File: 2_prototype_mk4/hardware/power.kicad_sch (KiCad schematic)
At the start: 8 parts, among them J2 Conn_01x04_Pin, J6 171825-4

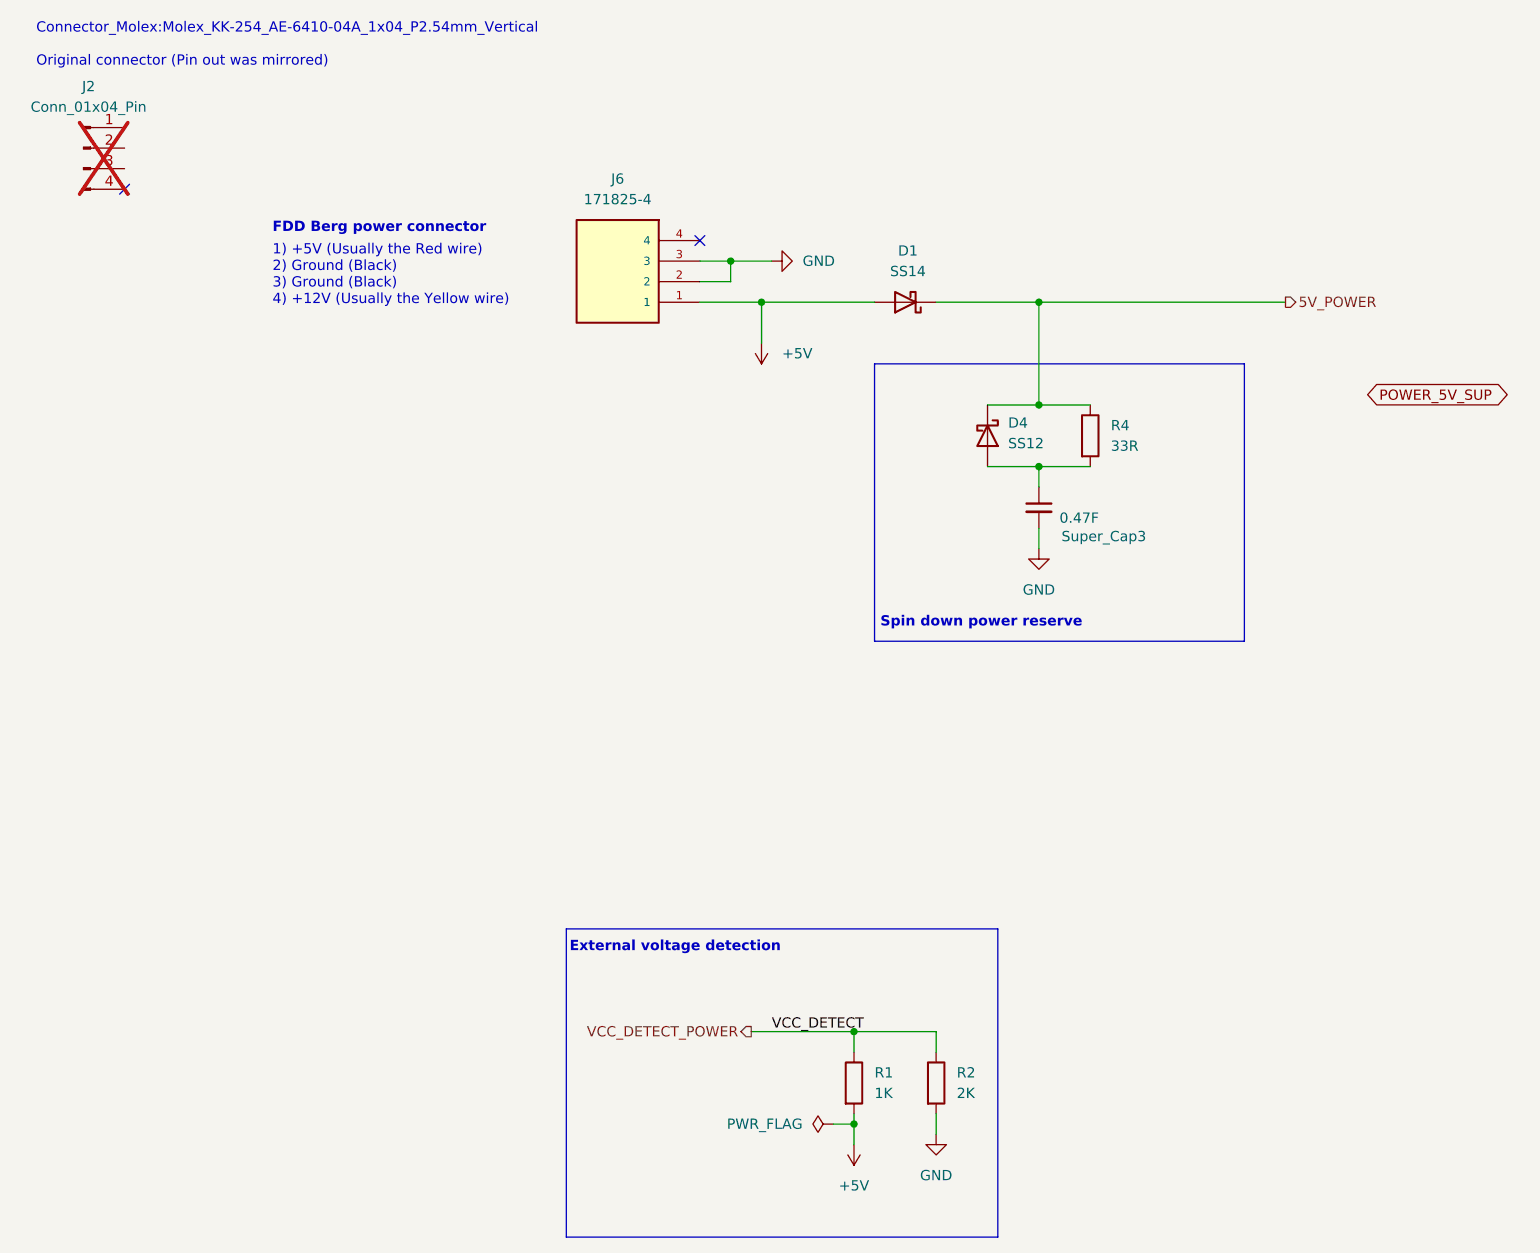
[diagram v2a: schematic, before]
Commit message: Fixed all Electrical Rule Check errors
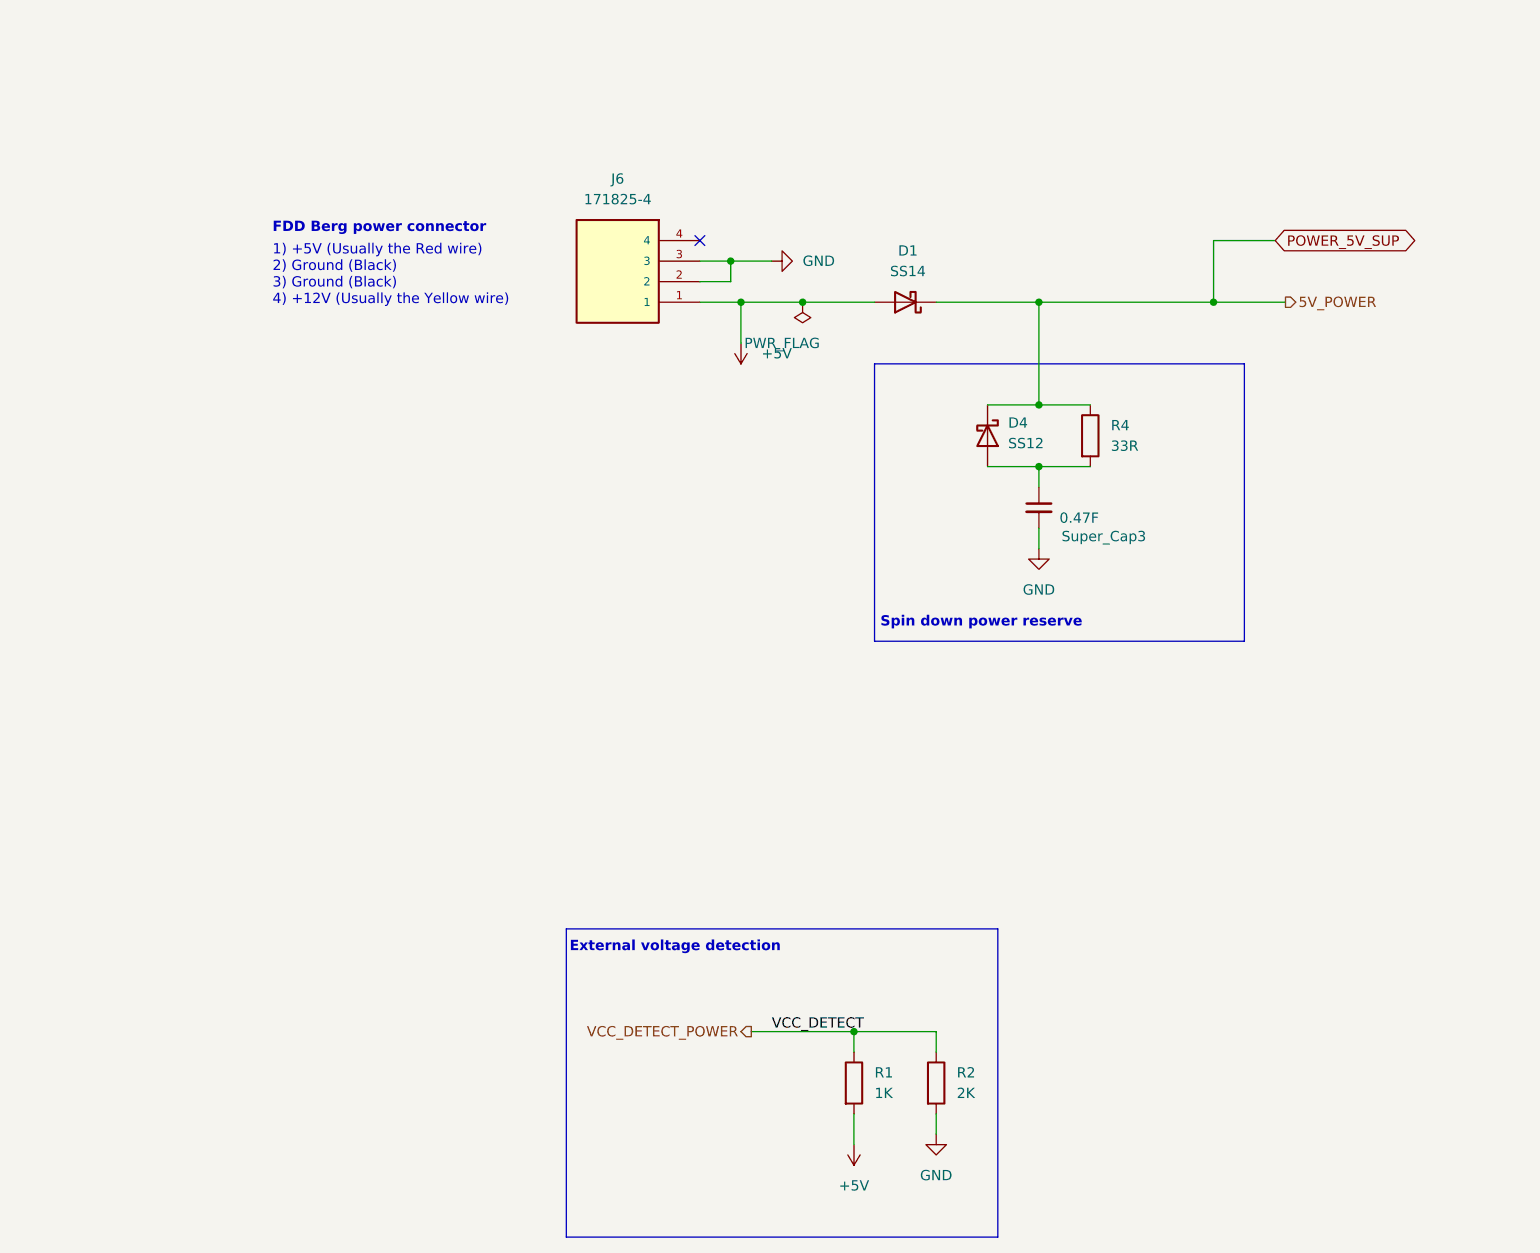
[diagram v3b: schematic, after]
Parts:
- removed J2: Conn_01x04_Pin, Connector_Molex:Molex_KK-254_AE-6410-04A_1x04_P2.54mm_Vertical, symbol Connector:Conn_01x04_Pin
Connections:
- net 5V_POWER is gone; now on net POWER_5V_SUP: D1.1 (K), D4.1 (K), R4.1
- no-connect marks 2 -> 1
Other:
- note removed: "Connector_Molex:Molex_KK-254_AE-6410-04A_1x04_P2.54mm_Vertical Original connector (Pin out was mirrored)"
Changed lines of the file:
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@@
-		)
-	)
-	(text "Connector_Molex:Molex_KK-254_AE-6410-04A_1x04_P2.54mm_Vertical\n\nOriginal connector (Pin out was mirrored)"
-		(exclude_from_sim no)
-		(at 37.338 41.91 0)
-		(effects
-			(font
-				(size 1.27 1.27)
-			)
-			(justify left)
 		)
 	)
@@
 	)
 	(junction
-		(at 138.43 175.26)
+		(at 138.43 163.83)
 		(diameter 0)
 		(color 0 0 0 0)
 	)
 	(junction
-		(at 138.43 163.83)
+		(at 182.88 73.66)
+		(diameter 0)
+		(color 0 0 0 0)
+	)
+	(junction
+		(at 124.46 73.66)
 		(diameter 0)
 		(color 0 0 0 0)
@@
 	)
 	(junction
-		(at 127 73.66)
-		(diameter 0)
-		(color 0 0 0 0)
-	)
-	(junction
 		(at 161.29 86.36)
 		(diameter 0)
@@
 		(color 0 0 0 0)
 	)
-	(no_connect
-		(at 48.26 59.69)
+	(junction
+		(at 132.08 73.66)
+		(diameter 0)
+		(color 0 0 0 0)
 	)
 	(no_connect
@@
 	(wire
 		(pts
-			(xy 138.43 175.26) (xy 138.43 173.99)
+			(xy 182.88 66.04) (xy 190.5 66.04)
+		)
+		(stroke
+			(width 0)
+			(type default)
+		)
+	)
+	(wire
+		(pts
+			(xy 138.43 173.99) (xy 138.43 177.8)
+		)
+		(stroke
+			(width 0)
+			(type default)
+		)
+	)
+	(wire
+		(pts
+			(xy 182.88 73.66) (xy 191.77 73.66)
 		)
 		(stroke
@@
 	(wire
 		(pts
-			(xy 161.29 73.66) (xy 191.77 73.66)
-		)
-		(stroke
-			(width 0)
-			(type default)
-		)
-	)
-	(wire
-		(pts
-			(xy 127 73.66) (xy 140.97 73.66)
+			(xy 161.29 73.66) (xy 182.88 73.66)
 		)
 		(stroke
@@
 	(wire
 		(pts
-			(xy 127 78.74) (xy 127 73.66)
+			(xy 124.46 73.66) (xy 132.08 73.66)
+		)
+		(stroke
+			(width 0)
+			(type default)
+		)
+	)
+	(wire
+		(pts
+			(xy 124.46 78.74) (xy 124.46 73.66)
 		)
 		(stroke
@@
 	(wire
 		(pts
-			(xy 119.38 73.66) (xy 127 73.66)
+			(xy 119.38 73.66) (xy 124.46 73.66)
 		)
 		(stroke
@@
 	(wire
 		(pts
+			(xy 132.08 73.66) (xy 140.97 73.66)
+		)
+		(stroke
+			(width 0)
+			(type default)
+		)
+	)
+	(wire
+		(pts
+			(xy 182.88 66.04) (xy 182.88 73.66)
+		)
+		(stroke
+			(width 0)
+			(type default)
+		)
+	)
+	(wire
+		(pts
 			(xy 161.29 93.98) (xy 167.64 93.98)
-		)
-		(stroke
-			(width 0)
-			(type default)
-		)
-	)
-	(wire
-		(pts
-			(xy 138.43 175.26) (xy 138.43 177.8)
-		)
-		(stroke
-			(width 0)
-			(type default)
-		)
-	)
-	(wire
-		(pts
-			(xy 135.89 175.26) (xy 138.43 175.26)
 		)
 		(stroke
@@
 	(global_label "POWER_5V_SUP"
 		(shape bidirectional)
-		(at 201.93 85.09 0)
+		(at 190.5 66.04 0)
 		(fields_autoplaced yes)
 		(effects
@@
 		)
 		(property "Intersheetrefs" "${INTERSHEET_REFS}"
-			(at 220.5407 85.09 0)
+			(at 209.1107 66.04 0)
 			(hide yes)
 			(show_name no)
@@
 		(length 2.54)
 		(shape round)
-		(at 138.43 175.26 90)
+		(at 135.89 73.66 0)
 		(fields_autoplaced yes)
 		(effects
@@
 			(justify left bottom)
 		)
-		(property "Net Class" "POWER_5v"
-			(at 135.89 174.5615 90)
+		(property "Net Class" "Power"
+			(at 136.5885 71.12 0)
 			(show_name no)
 			(do_not_autoplace no)
@@
 		)
 		(property "Component Class" ""
-			(at -99.06 36.83 0)
+			(at -81.28 -2.54 0)
 			(show_name no)
 			(do_not_autoplace no)
@@
 		(length 2.54)
 		(shape round)
-		(at 165.1 93.98 180)
-		(effects
-			(font
-				(size 1.27 1.27)
-			)
-			(justify right bottom)
-		)
-		(property "Net Class" "POWER_5V_SUP"
-			(at 165.7985 96.52 0)
+		(at 171.45 73.66 0)
+		(fields_autoplaced yes)
+		(effects
+			(font
+				(size 1.27 1.27)
+			)
+			(justify left bottom)
+		)
+		(property "Net Class" "Power"
+			(at 172.1485 71.12 0)
 			(show_name no)
 			(do_not_autoplace no)
@@
 		)
 		(property "Component Class" ""
-			(at -41.91 8.89 0)
+			(at -52.07 1.27 0)
 			(show_name no)
 			(do_not_autoplace no)
@@
 	(symbol
 		(lib_id "power:+5V")
-		(at 127 78.74 180)
+		(at 124.46 78.74 180)
 		(unit 1)
 		(body_style 1)
@@
 		(fields_autoplaced yes)
 		(property "Reference" "#PWR014"
-			(at 127 74.93 0)
+			(at 124.46 74.93 0)
 			(hide yes)
 			(show_name no)
@@
 		)
 		(property "Value" "+5V"
-			(at 129.54 80.0099 0)
+			(at 127 80.0099 0)
 			(show_name no)
 			(do_not_autoplace no)
@@
 		)
 		(property "Footprint" ""
-			(at 127 78.74 0)
+			(at 124.46 78.74 0)
 			(hide yes)
 			(show_name no)
@@
 		)
 		(property "Datasheet" ""
-			(at 127 78.74 0)
+			(at 124.46 78.74 0)
 			(hide yes)
 			(show_name no)
@@
 		)
 		(property "Description" "Power symbol creates a global label with name \"+5V\""
-			(at 127 78.74 0)
+			(at 124.46 78.74 0)
 			(hide yes)
 			(show_name no)
@@
 	(symbol
 		(lib_id "power:PWR_FLAG")
-		(at 135.89 175.26 90)
+		(at 132.08 73.66 180)
 		(unit 1)
 		(body_style 1)
@@
 		(dnp no)
 		(property "Reference" "#FLG01"
-			(at 133.985 175.26 0)
+			(at 132.08 75.565 0)
 			(hide yes)
 			(show_name no)
@@
 		)
 		(property "Value" "PWR_FLAG"
-			(at 132.08 175.2599 90)
-			(show_name no)
-			(do_not_autoplace no)
-			(effects
-				(font
-					(size 1.27 1.27)
-				)
-				(justify left)
+			(at 129.54 78.74 0)
+			(show_name no)
+			(do_not_autoplace no)
+			(effects
+				(font
+					(size 1.27 1.27)
+				)
 			)
 		)
 		(property "Footprint" ""
-			(at 135.89 175.26 0)
+			(at 132.08 73.66 0)
 			(hide yes)
 			(show_name no)
@@
 		)
 		(property "Datasheet" ""
-			(at 135.89 175.26 0)
+			(at 132.08 73.66 0)
 			(hide yes)
 			(show_name no)
@@
 		)
 		(property "Description" "Special symbol for telling ERC where power comes from"
-			(at 135.89 175.26 0)
+			(at 132.08 73.66 0)
 			(hide yes)
 			(show_name no)
@@
 					(unit 1)
 				)
-			)
-		)
-	)
-	(symbol
-		(lib_id "Connector:Conn_01x04_Pin")
-		(at 43.18 54.61 0)
-		(unit 1)
-		(body_style 1)
-		(exclude_from_sim yes)
-		(in_bom no)
-		(on_board no)
-		(in_pos_files no)
-		(dnp yes)
-		(fields_autoplaced yes)
-		(property "Reference" "J2"
-			(at 43.815 46.99 0)
-			(show_name no)
-			(do_not_autoplace no)
-			(effects
-				(font
-					(size 1.27 1.27)
-				)
-			)
-		)
-		(property "Value" "Conn_01x04_Pin"
-			(at 43.815 49.53 0)
-			(show_name no)
-			(do_not_autoplace no)
-			(effects
-				(font
-					(size 1.27 1.27)
-				)
-			)
-		)
-		(property "Footprint" "Connector_Molex:Molex_KK-254_AE-6410-04A_1x04_P2.54mm_Vertical"
-			(at 43.18 54.61 0)
-			(hide yes)
-			(show_name no)
-			(do_not_autoplace no)
-			(effects
-				(font
-					(size 1.27 1.27)
-				)
-			)
-		)
-		(property "Datasheet" ""
-			(at 43.18 54.61 0)
-			(hide yes)
-			(show_name no)
-			(do_not_autoplace no)
-			(effects
-				(font
-					(size 1.27 1.27)
-				)
-			)
-		)
-		(property "Description" "Generic connector, single row, 01x04, script generated"
-			(at 43.18 54.61 0)
-			(hide yes)
-			(show_name no)
-			(do_not_autoplace no)
-			(effects
-				(font
-					(size 1.27 1.27)
-				)
-			)
-		)
-		(pin "3"
-		)
-		(pin "4"
-		)
-		(pin "1"
-		)
-		(pin "2"
-		)
-		(instances
-			(project "HDD Synth Prototype MK4"
-				(path "/1a22431a-ba36-40a0-9a7e-c2a82ec69c53/045d9081-4e75-4a6b-9321-784f56d8310c"
-					(reference "J2")
-					(unit 1)
-				)
-			)
-			(project "FDD Synth prototype MK1"
-				(path "/ed113b11-1722-4efb-9669-9e8c19f5c8fd/c4fff946-c3ba-4a7b-ae26-49b27e5a2cee"
-					(reference "J4")
-					(unit 1)
-				)

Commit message: MK4 PCB layout complete
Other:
- note added: "https://www.snapeda.com/parts/171825-4/TE%20Connectivity%20AMP%20Connectors/view-part/"
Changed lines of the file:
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@@
+		)
+	)
+	(text "https://www.snapeda.com/parts/171825-4/TE%20Connectivity%20AMP%20Connectors/view-part/"
+		(exclude_from_sim no)
+		(at 108.458 51.816 0)
+		(effects
+			(font
+				(size 1.27 1.27)
+			)
 		)
 	)
@@
 		)
 	)
+	(netclass_flag ""
+		(length 2.54)
+		(shape round)
+		(at 163.83 93.98 180)
+		(fields_autoplaced yes)
+		(effects
+			(font
+				(size 1.27 1.27)
+			)
+			(justify right bottom)
+		)
+		(property "Net Class" "Power"
+			(at 164.5285 96.52 0)
+			(show_name no)
+			(do_not_autoplace no)
+			(effects
+				(font
+					(size 1.27 1.27)
+				)
+				(justify left)
+			)
+		)
+		(property "Component Class" ""
+			(at -43.18 6.35 0)
+			(show_name no)
+			(do_not_autoplace no)
+			(effects
+				(font
+					(size 1.27 1.27)
+					(italic yes)
+				)
+			)
+		)
+	)

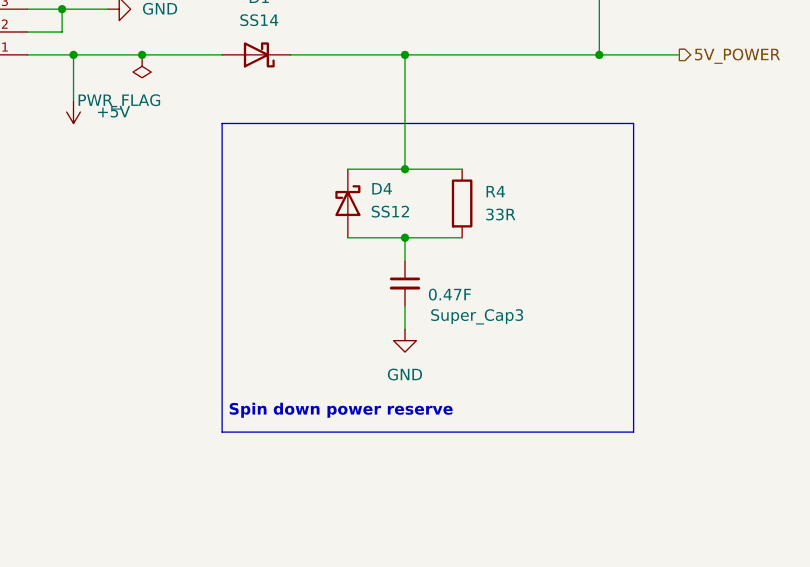
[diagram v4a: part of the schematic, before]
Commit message: Update MKIV hardware & use MKIII software as basic for MKIV
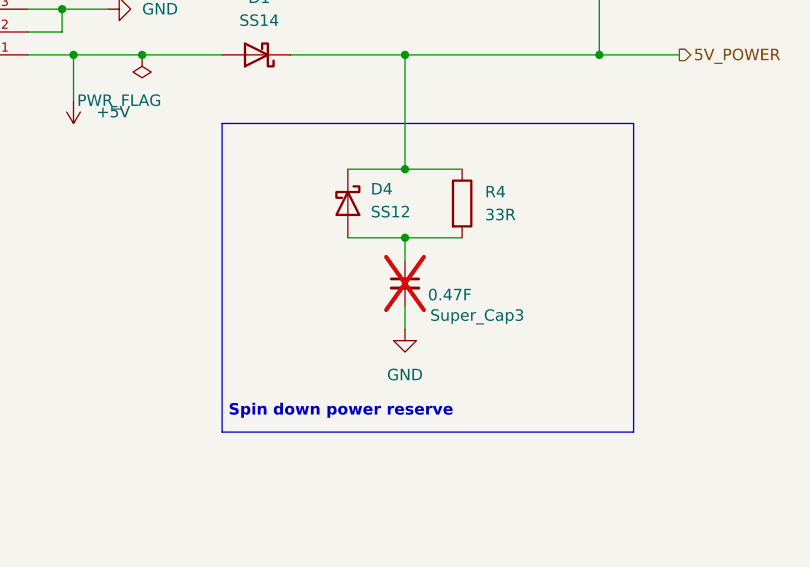
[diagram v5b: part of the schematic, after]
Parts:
- D4: Manufacturer onsemi / Taiwan Semi -> (none)
- R4: Manufacturer_Part_Number RC1206FR-0733RL -> RC0603FR-0733RL
- Super_Cap3: now not fitted; now left out of the parts list
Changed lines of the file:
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@@
 		(body_style 1)
 		(exclude_from_sim no)
-		(in_bom yes)
+		(in_bom no)
 		(on_board yes)
 		(in_pos_files yes)
-		(dnp no)
+		(dnp yes)
 		(property "Reference" "Super_Cap3"
 			(at 164.084 102.616 0)
@@
 		)
 		(property "Manufacturer_Part_Number" "DX-5R5V474U"
-			(at 161.29 99.06 0)
-			(hide yes)
-			(show_name no)
-			(do_not_autoplace no)
-			(effects
-				(font
-					(size 1.27 1.27)
-				)
-			)
-		)
-		(property "Manufacturer" ""
 			(at 161.29 99.06 0)
 			(hide yes)
@@
 			)
 		)
-		(property "Manufacturer_Part_Number" "RC1206FR-0733RL"
-			(at 167.64 90.17 0)
-			(hide yes)
-			(show_name no)
-			(do_not_autoplace no)
-			(effects
-				(font
-					(size 1.27 1.27)
-				)
-			)
-		)
-		(property "Manufacturer" ""
+		(property "Manufacturer_Part_Number" "RC0603FR-0733RL"
 			(at 167.64 90.17 0)
 			(hide yes)
@@
 			)
 		)
-		(property "Manufacturer" "onsemi / Taiwan Semi"
-			(at 154.94 90.17 90)
-			(hide yes)
-			(show_name no)
-			(do_not_autoplace no)
-			(effects
-				(font
-					(size 1.27 1.27)
-				)
-			)
-		)
 		(property "LCSC_Part_Number" "C184027"
 			(at 154.94 90.17 90)
@@
 			)
 		)
-		(property "Manufacturer" ""
-			(at 138.43 170.18 0)
-			(hide yes)
-			(show_name no)
-			(do_not_autoplace no)
-			(effects
-				(font
-					(size 1.27 1.27)
-				)
-			)
-		)
 		(property "LCSC_Part_Number" ""
 			(at 138.43 170.18 0)
@@
 			(at 148.59 170.18 0)
 			(hide yes)
-			(show_name no)
-			(do_not_autoplace no)
-			(effects
-				(font
-					(size 1.27 1.27)
-				)
-			)
-		)
-		(property "Manufacturer" ""
-			(at 148.59 170.18 0)
-			(hide yes)

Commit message: Final MKIV tweaks before sending off to PCBWay
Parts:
- Super_Cap3: value 0.47F -> 1F; footprint Capacitor_THT:CP_Radial_D12.5mm_P5.00mm -> Capacitor_THT:CP_Radial_D14.0mm_P5.00mm; Manufacturer_Part_Number DX-5R5V474U -> (none); now fitted; now in the parts list
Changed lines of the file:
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@@
 		(body_style 1)
 		(exclude_from_sim no)
-		(in_bom no)
+		(in_bom yes)
 		(on_board yes)
 		(in_pos_files yes)
-		(dnp yes)
+		(dnp no)
 		(property "Reference" "Super_Cap3"
 			(at 164.084 102.616 0)
@@
 			)
 		)
-		(property "Value" "0.47F"
+		(property "Value" "1F"
 			(at 163.83 100.3362 0)
 			(show_name no)
@@
 			)
 		)
-		(property "Footprint" "Capacitor_THT:CP_Radial_D12.5mm_P5.00mm"
+		(property "Footprint" "Capacitor_THT:CP_Radial_D14.0mm_P5.00mm"
 			(at 161.29 99.06 0)
 			(hide yes)
@@
 			)
 		)
-		(property "Datasheet" ""
+		(property "Datasheet" "https://resources.kitronik.co.uk/pdf/super_capacitor.pdf"
 			(at 161.29 99.06 0)
 			(hide yes)
@@
 			)
 		)
-		(property "Description" "Unpolarized capacitor, small symbol"
+		(property "Description" "polarized radial super capacitor, 1F 5.5V"
 			(at 161.29 99.06 0)
 			(hide yes)
@@
 			)
 		)
-		(property "Manufacturer_Part_Number" "DX-5R5V474U"
+		(property "Manufacturer_Part_Number" ""
 			(at 161.29 99.06 0)
 			(hide yes)

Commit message: MKIV tweaks
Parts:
- R4: Manufacturer_Part_Number RC0603FR-0733RL -> SR1206FR-7W33RL
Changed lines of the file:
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@@
 			)
 		)
-		(property "Description" "Resistor"
+		(property "Description" "Resistor 33 OHM 1% 1/2W 1206 ANTI-SURGE"
 			(at 167.64 90.17 0)
 			(hide yes)
@@
 			)
 		)
-		(property "Manufacturer_Part_Number" "RC0603FR-0733RL"
+		(property "Manufacturer_Part_Number" "SR1206FR-7W33RL"
 			(at 167.64 90.17 0)
 			(hide yes)
